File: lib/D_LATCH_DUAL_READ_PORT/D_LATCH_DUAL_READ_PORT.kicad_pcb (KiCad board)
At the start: 2 copper layers, 18 parts

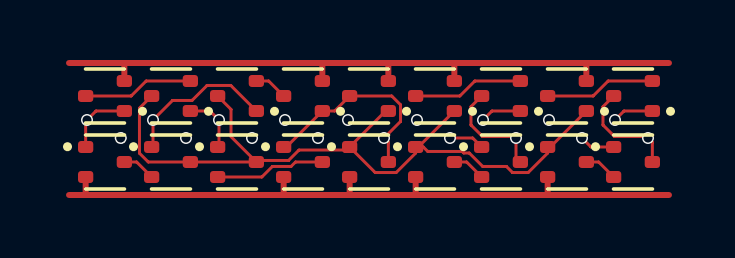
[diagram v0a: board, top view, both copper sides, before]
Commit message: All cells now use 1mm*4mm grid rather than 1.1mm*4.4mm
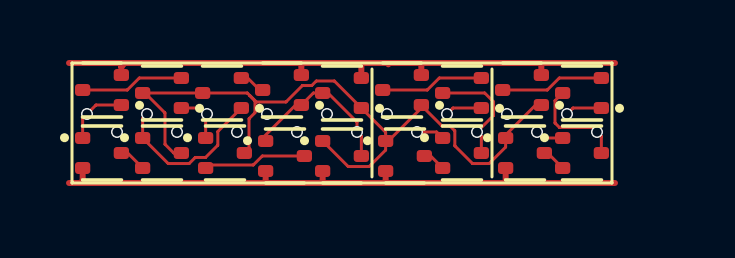
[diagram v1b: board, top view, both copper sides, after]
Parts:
- moved port2.N2 1.73 mm to (17.0, 3.00)
- moved port2.P2 1.70 mm to (17.0, 1.00)
- moved port2.P1 1.51 mm to (15.0, 0.90)
- moved port2.N1 1.43 mm to (15.1, 3.00)
- moved port1.N2 1.33 mm to (13.0, 3.00)
- moved port1.P2 1.30 mm to (13.0, 1.00)
- moved port1.P1 1.12 mm to (11.0, 0.90)
- moved port1.N1 1.02 mm to (11.1, 3.10)
- moved latch.NOT2.N1 0.92 mm to (9.00, 3.10)
- moved latch.NOT2.P1 0.91 mm to (9.00, 1.00)
- moved latch.NOT3.P1 0.73 mm to (7.00, 0.90)
- moved latch.NOT3.N1 0.63 mm to (7.10, 3.10)
- moved latch.NOT3.P2 0.51 mm to (5.00, 1.00)
- moved latch.NOT3.N2 0.50 mm to (5.10, 3.00)
- moved latch.NOT1.N2 0.42 mm to (3.00, 3.00)
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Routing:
- net VDD: track 23.1 -> 20.6 mm
- net GND: track 23.1 -> 20.6 mm
- net Q: track 6.92 -> 5.36 mm
- net latch.NOT1.Y: track 26.0 -> 25.2 mm

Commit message: Make the pads of my SOT523 footprint very slightly smaller, which is enough to route all the cells and leave the mosfets exactly on the grid
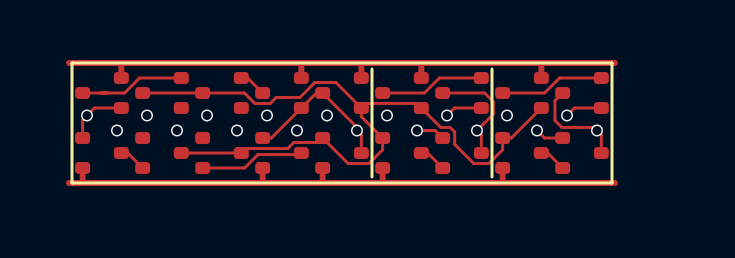
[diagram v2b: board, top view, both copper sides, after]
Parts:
- latch.NOT1.N1, latch.NOT1.N2, latch.NOT1.P1, latch.NOT1.P2, latch.NOT2.N1, latch.NOT2.P1, latch.NOT3.N1, latch.NOT3.N2, latch.NOT3.P1, latch.NOT3.P2, port1.N1, port1.N2, port1.P1, port1.P2, port2.N1, port2.N2, port2.P1, port2.P2: footprint Package_TO_SOT_SMD:SOT-523 -> RV523:SOT523
- moved latch.NOT3.N1 0.14 mm to (7.00, 3.00)
- moved port1.N1 0.14 mm to (11.0, 3.00)
- moved latch.NOT2.N1 0.10 mm to (9.00, 3.00)
- moved latch.NOT1.P1 0.10 mm to (1.00, 1.00)
- moved latch.NOT3.P1 0.10 mm to (7.00, 1.00)
- moved port1.P1 0.10 mm to (11.0, 1.00)
- moved port2.P1 0.10 mm to (15.0, 1.00)
- moved latch.NOT3.N2 0.10 mm to (5.00, 3.00)
- moved port2.N1 0.10 mm to (15.0, 3.00)
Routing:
- net CLK: track 5.54 -> 0.00 mm
- net nCLK: track 1.76 -> 0.00 mm

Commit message: Propagate MOSFET values to the cells' PCBs
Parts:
- latch.NOT1.N1, latch.NOT1.N2, latch.NOT2.N1, latch.NOT3.N1, latch.NOT3.N2, port1.N1, port1.N2, port2.N1, port2.N2: value (none) -> NMOS
- latch.NOT1.P1, latch.NOT1.P2, latch.NOT2.P1, latch.NOT3.P1, latch.NOT3.P2, port1.P1, port1.P2, port2.P1, port2.P2: value (none) -> PMOS
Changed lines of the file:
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@@
 			)
 		)
-		(property "Value" ""
+		(property "Value" "PMOS"
 			(at 0 0 180)
 			(layer "F.Fab")
@@
 			)
 		)
-		(property "Value" ""
+		(property "Value" "PMOS"
 			(at 0 0 180)
 			(layer "F.Fab")
@@
 			)
 		)
-		(property "Value" ""
+		(property "Value" "PMOS"
 			(at 0 0 180)
 			(layer "F.Fab")
@@
 			)
 		)
-		(property "Value" ""
+		(property "Value" "PMOS"
 			(at 0 0 180)
 			(layer "F.Fab")
@@
 			)
 		)
-		(property "Value" ""
+		(property "Value" "NMOS"
 			(at 0 0 0)
 			(layer "F.Fab")
@@
 			)
 		)
-		(property "Value" ""
+		(property "Value" "NMOS"
 			(at 0 0 0)
 			(layer "F.Fab")
@@
 			)
 		)
-		(property "Value" ""
+		(property "Value" "PMOS"
 			(at 0 0 180)
 			(layer "F.Fab")
@@
 			)
 		)
-		(property "Value" ""
+		(property "Value" "NMOS"
 			(at 0 0 0)
 			(layer "F.Fab")
@@
 			)
 		)
-		(property "Value" ""
+		(property "Value" "NMOS"
 			(at 0 0 0)
 			(layer "F.Fab")
@@
 			)
 		)
-		(property "Value" ""
+		(property "Value" "NMOS"
 			(at 0 0 0)
 			(layer "F.Fab")
@@
 			)
 		)
-		(property "Value" ""
+		(property "Value" "NMOS"
 			(at 0 0 0)
 			(layer "F.Fab")
@@
 			)
 		)
-		(property "Value" ""
+		(property "Value" "PMOS"
 			(at 0 0 180)
 			(layer "F.Fab")
@@
 			)
 		)
-		(property "Value" ""
+		(property "Value" "PMOS"
 			(at 0 0 180)
 			(layer "F.Fab")
@@
 			)
 		)
-		(property "Value" ""
+		(property "Value" "PMOS"
 			(at 0 0 180)
 			(layer "F.Fab")
@@
 			)
 		)
-		(property "Value" ""
+		(property "Value" "PMOS"
 			(at 0 0 180)
 			(layer "F.Fab")
@@
 			)
 		)
-		(property "Value" ""
+		(property "Value" "NMOS"
 			(at 0 0 0)
 			(layer "F.Fab")
@@
 			)
 		)
-		(property "Value" ""
+		(property "Value" "NMOS"
 			(at 0 0 0)
 			(layer "F.Fab")
@@
 			)
 		)
-		(property "Value" ""
-			(at 0 0 0)
-			(layer "F.Fab")
+		(property "Value" "NMOS"
+			(at 0 0 0)
+			(layer "F.Fab")

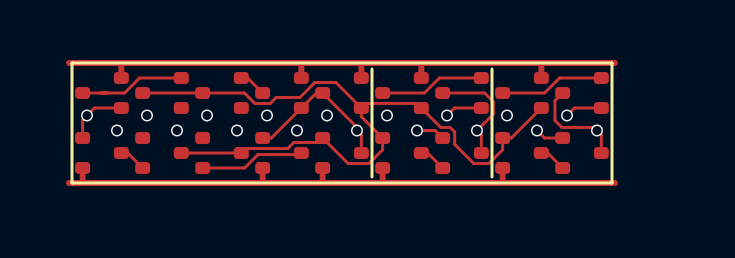
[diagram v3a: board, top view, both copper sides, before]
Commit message: D_LATCH_DUAL_READ_PORT.kicad_pcb: some missing tracks
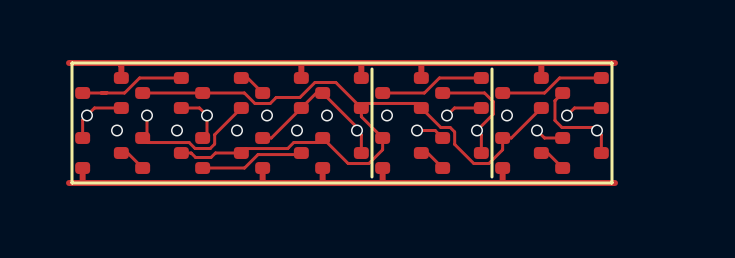
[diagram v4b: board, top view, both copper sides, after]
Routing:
- net CLK: track 0.00 -> 4.99 mm
- net nCLK: track 0.00 -> 1.77 mm
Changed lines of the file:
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@@
 		(net 5)
+	)
+	(segment
+		(start 2.5 1.75)
+		(end 2.5 2.355)
+		(width 0.1)
+		(layer "F.Cu")
+		(net 6)
+	)
+	(segment
+		(start 4.756 2.389)
+		(end 4.756 2.700812)
+		(width 0.1)
+		(layer "F.Cu")
+		(net 6)
+	)
+	(segment
+		(start 4.104242 2.85)
+		(end 3.905242 2.651)
+		(width 0.1)
+		(layer "F.Cu")
+		(net 6)
+	)
+	(segment
+		(start 2.5 2.355)
+		(end 2.355 2.5)
+		(width 0.1)
+		(layer "F.Cu")
+		(net 6)
+	)
+	(segment
+		(start 2.506 2.651)
+		(end 2.355 2.5)
+		(width 0.1)
+		(layer "F.Cu")
+		(net 6)
+	)
+	(segment
+		(start 4.606812 2.85)
+		(end 4.104242 2.85)
+		(width 0.1)
+		(layer "F.Cu")
+		(net 6)
+	)
+	(segment
+		(start 4.756 2.700812)
+		(end 4.606812 2.85)
+		(width 0.1)
+		(layer "F.Cu")
+		(net 6)
+	)
+	(segment
+		(start 3.905242 2.651)
+		(end 2.506 2.651)
+		(width 0.1)
+		(layer "F.Cu")
+		(net 6)
+	)
+	(segment
+		(start 5.645 1.5)
+		(end 4.756 2.389)
+		(width 0.1)
+		(layer "F.Cu")
+		(net 6)
 	)
 	(via
@@
 	)
 	(segment
+		(start 4.121399 3.15)
+		(end 4.632842 3.15)
+		(width 0.1)
+		(layer "F.Cu")
+		(net 7)
+	)
+	(segment
+		(start 3.645 3)
+		(end 3.971399 3)
+		(width 0.1)
+		(layer "F.Cu")
+		(net 7)
+	)
+	(segment
 		(start 8.355 2.5)
 		(end 8.2055 2.6495)
@@
 	)
 	(segment
+		(start 4.782842 3)
+		(end 5.645 3)
+		(width 0.1)
+		(layer "F.Cu")
+		(net 7)
+	)
+	(segment
 		(start 13.393688 3.3505)
 		(end 13.896312 3.3505)
@@
 	)
 	(segment
-		(start 3.645 3)
-		(end 5.645 3)
-		(width 0.1)
-		(layer "F.Cu")
-		(net 7)
-	)
-	(segment
 		(start 14.355 2.891812)
 		(end 14.355 2.5)
@@
 	)
 	(segment
+		(start 4.632842 3.15)
+		(end 4.782842 3)
+		(width 0.1)
+		(layer "F.Cu")
+		(net 7)
+	)
+	(segment
 		(start 8.7945 0.6495)
 		(end 8.097312 0.6495)
@@
 	)
 	(segment
+		(start 3.971399 3)
+		(end 4.121399 3.15)
+		(width 0.1)
+		(layer "F.Cu")
+		(net 7)
+	)
+	(segment
 		(start 12.2945 2.1495)
 		(end 12.606312 2.1495)
@@
 		(net 8)
 	)
+	(segment
+		(start 4.25 1.5)
+		(end 4.5 1.75)
+		(width 0.1)
+		(layer "F.Cu")
+		(net 9)
+	)
+	(segment
+		(start 3.645 1.5)
+		(end 4.25 1.5)
+		(width 0.1)
+		(layer "F.Cu")
+		(net 9)
+	)
+	(segment
+		(start 4.5 1.75)
+		(end 4.5 2.355)
+		(width 0.1)
+		(layer "F.Cu")
+		(net 9)
+	)
+	(segment
+		(start 4.5 2.355)
+		(end 4.355 2.5)
+		(width 0.1)
+		(layer "F.Cu")
+		(net 9)
+	)
 	(via
